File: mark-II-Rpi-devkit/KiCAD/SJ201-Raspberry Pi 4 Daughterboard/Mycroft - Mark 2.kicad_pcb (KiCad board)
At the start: 4 copper layers, 72 x 93 mm, 210 parts, among them J1 Barrel_Jack, J10 Debug Connector, J11 I2S, J2 PVDD Jumper, J3 SPKLEFT, J4 SPKRIGHT, J5 PowerTP, J6 Raspberry_Pi_4, J7 USB_B_Micro, J8 MIC, J9 AudioJack3_Ground_Switch, P1 LED, P2 LED, P3 LED, P4 LED, Q3 AO3415A, Q4 FDV301N, SW1 MuteMic, U1 XL4501E1, U10 SPK0838HT4H-1, U11 SPK0838HT4H-1, U12 NCP303LSN30, U13 CM108B, U3 MAX9744, U4 AZ1117CH-3.3, U5 SN74LVC125APWR, U6 FE1.1s, U7 MP2359, U8 XMOS-XVF3510, U9 AT25SF161 16MBIT, X1 SG-210STF 24M, Y2 12MHz

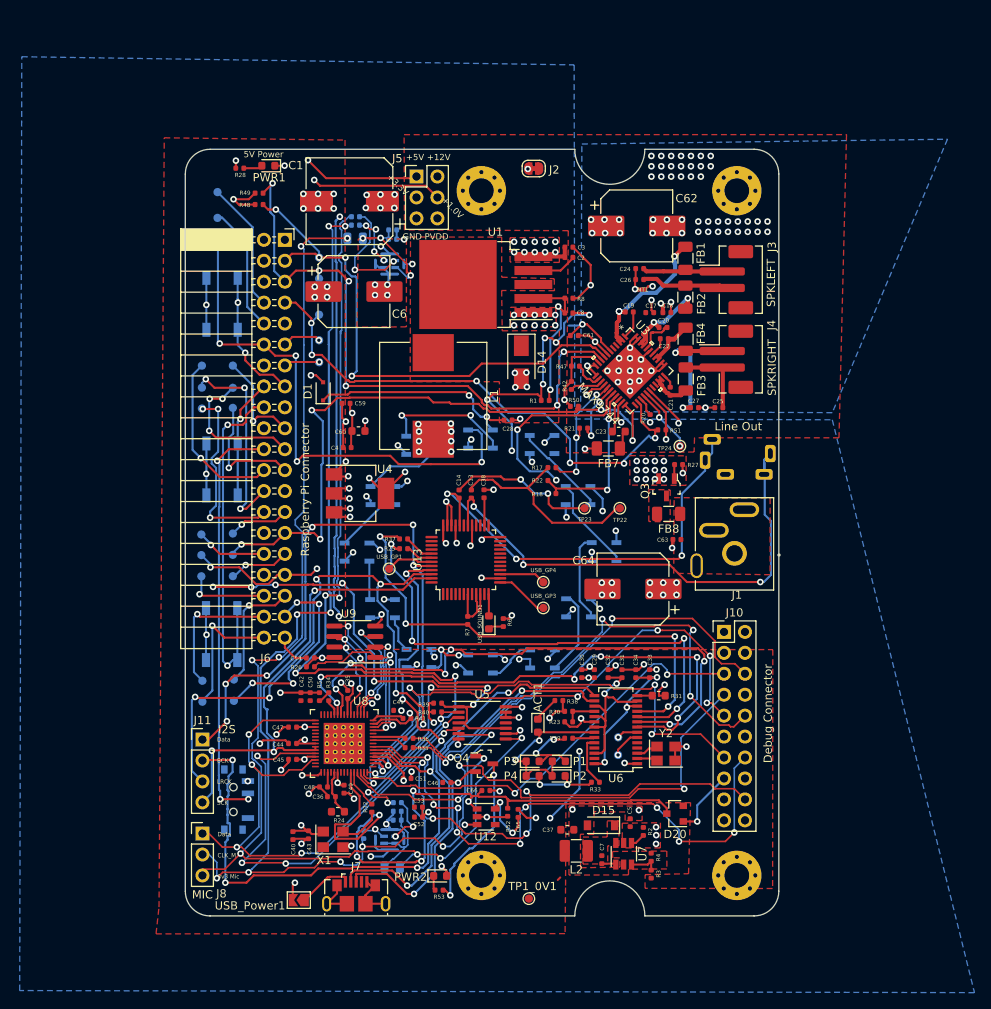
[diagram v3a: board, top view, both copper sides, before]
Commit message: Change vertical barrel connector, files sent to JLC PCB for printing and assembly.
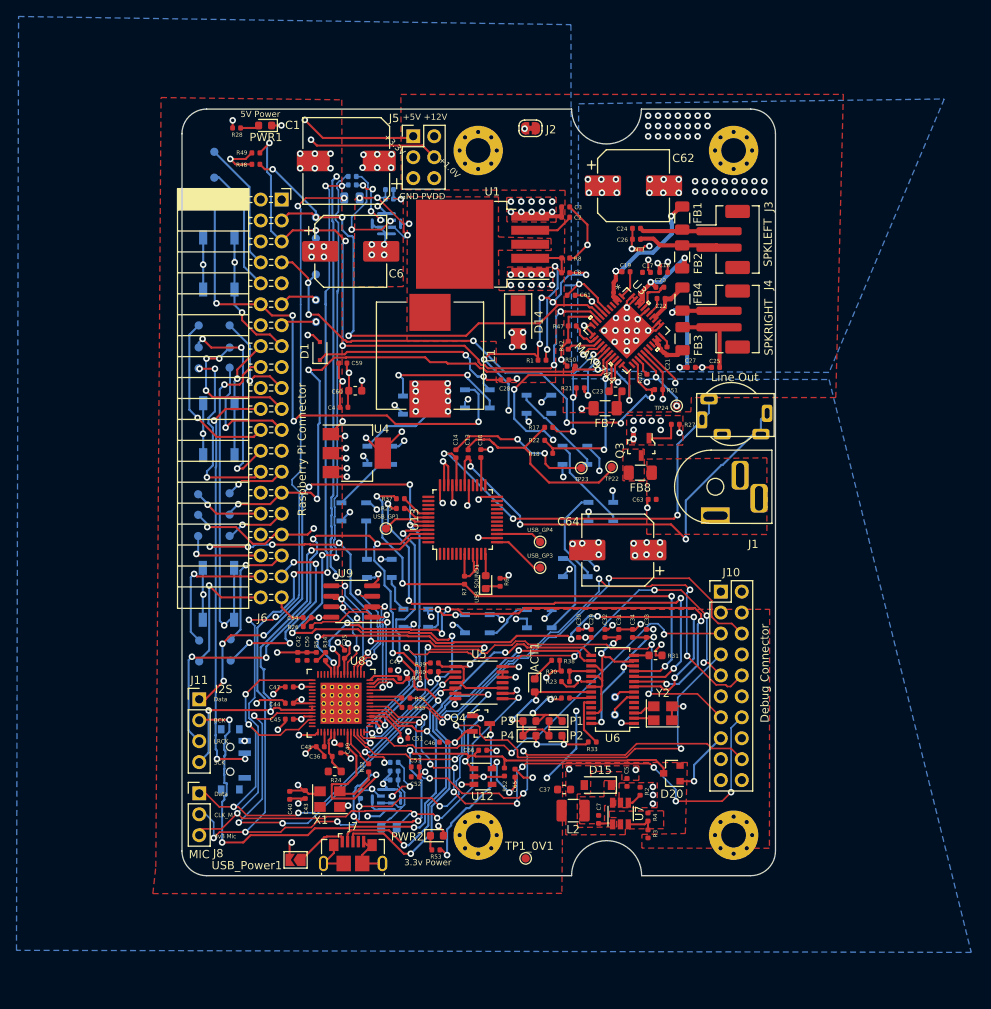
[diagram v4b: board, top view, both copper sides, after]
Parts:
- J1: footprint mycroft:CUI_PJ-090H -> user:BarrelJack_Vertical
- moved J1 8.41 mm to (64.7, 45.8), turned to 90 degrees
- moved FB8 6.07 mm to (55.6, 44.1)
- moved Q3 5.78 mm to (55.7, 41.0)
- moved C63 5.72 mm to (57.0, 47.4)
- moved TP22 5.10 mm to (52.1, 43.4)
- moved C64 5.07 mm to (52.9, 53.5)
- moved C40 4.90 mm to (13.1, 83.3)
- moved C44 4.90 mm to (13.0, 72.1)
- moved C46 4.90 mm to (31.7, 76.8)
- moved C52 4.90 mm to (28.3, 81.0)
- moved C65 4.90 mm to (40.4, 80.6)
- moved C7 4.90 mm to (50.5, 86.2)
- moved D20 4.90 mm to (59.4, 80.6)
- moved D7 4.90 mm to (28.4, 61.8)
- moved FB6 4.90 mm to (25.1, 87.1)
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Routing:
- net VoutL: track 62.2 -> 55.0 mm
- net Net-(Q3-Pad1): track 1.81 -> 4.49 mm
- net Net-(D10-Pad2): track 10.7 -> 11.8 mm
- net +12V: vias 35 -> 30
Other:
- outline, holes or cut-outs redrawn
- board text added: "3.3v Power"
- board text added: "Mycroft MK2 v0.65 SJ201-01-01"
- board text removed: "Mycroft MK2 v0.64 SJ201-01-01"

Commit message: Mark 2 - PCB Files to the printer
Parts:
- U9: footprint Package_SO:SOIC-8_3.9x4.9mm_P1.27mm -> Package_SO:SOIC-8_5.23x5.23mm_P1.27mm
- moved C54 0.47 mm to (14.7, 61.7)
- moved R26 0.47 mm to (14.7, 62.8)
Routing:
- net I2S_LRCK: track 81.4 -> 85.1 mm
- net /xmos/QSPI_CS_N: track 21.0 -> 24.6 mm
- net /xmos/QSPI_D0: track 14.4 -> 16.6 mm
- net +3V3: track 86.0 -> 87.4 mm
- net GND: track 238.7 -> 237.6 mm
- net /xmos/QSPI_D3: track 10.7 -> 11.8 mm
- net /xmos/QSPI_D2: track 14.1 -> 15.1 mm
- net /xmos/QSPI_CLK: track 18.9 -> 19.8 mm
- net /xmos/QSPI_D1: track 11.7 -> 12.4 mm
